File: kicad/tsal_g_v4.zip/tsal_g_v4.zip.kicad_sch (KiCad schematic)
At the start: 91 parts, among them J1 Conn_01x02_Pin, J2 Conn_01x02_Pin, J3 Conn_01x06_Pin, J6 Conn_01x02_Pin, J7 Conn_01x02_Pin, J8 Conn_01x03, Q1 2N7002, Q2 NCE60P04R, U1 TL431DBZ, U10 BU4S01G2, U11 BU4S01G2, U14 BUS4S71G2, U15 BUS4S71G2, U16 BU4SU69G2, U17 40106, U18 BU4S01G2, U19 BU4S01G2, U2 LTV-817S, U20 4071, U3 B1212, U4 BU4SU69G2, U5 40106, U6 40106, U7 BU4S81G2

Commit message: updated tsal
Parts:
- removed C20: 0.1uF, Capacitor_SMD:C_0805_2012Metric_Pad1.18x1.45mm_HandSolder, symbol Device:C
- removed D8: LED, LED_SMD:LED_0805_2012Metric_Pad1.15x1.40mm_HandSolder, symbol Device:LED
- removed Q2: NCE60P04R, Package_TO_SOT_SMD:SOT-223-3_TabPin2, symbol Transistor_FET:AO3401A
- removed R27: 1k, Resistor_SMD:R_0805_2012Metric_Pad1.20x1.40mm_HandSolder, symbol Device:R
- removed U15: BUS4S71G2, Package_TO_SOT_SMD:SOT-23-5_HandSoldering, symbol 74xGxx:74AHC1G32
- removed U17: 40106, to be sorted:SOIC-14_3.9x8.7mm_P1.27mm_extendedpad, symbol 4xxx:40106
- removed U18, U19: BU4S01G2, Package_TO_SOT_SMD:SOT-23-5_HandSoldering, symbol 74xGxx:74AHC1G02
- added D10: LED, RMC_LED:LED_0805_2012Metric_Pad1.45x1.40mm_HandSolder, symbol Device:LED
- added Q4: QM6015D, RMC_TO:TO-252-2, symbol Transistor_FET:QM6015D
- added R31: 1k, RMC_Resistor:R_0805_2012Metric_Pad1.20x1.40mm_HandSolder_L, symbol Device:R
- added U12: 4077, RMC_SO:SOIC127P600X175-14N, symbol 4xxx:4077
- added U13: BU4S71G2, symbol 74xGxx:74AHC1G32
- added U9: 40106, RMC_SO:SOIC127P600X175-14N, symbol 4xxx:40106
- C1, C11, C12, C15, C16, C17, C18, C19, C2, C21, C22, C23, C24, C3, C4, C5, C6, C7, C8, C9: footprint Capacitor_SMD:C_0805_2012Metric_Pad1.18x1.45mm_HandSolder -> RMC_Capacitor:C_0805_2012Metric_Pad1.18x1.45mm_HandSolder_L
- D2, D4, D5, D6, D7, D9: footprint LED_SMD:LED_0805_2012Metric_Pad1.15x1.40mm_HandSolder -> RMC_LED:LED_0805_2012Metric_Pad1.45x1.40mm_HandSolder
- D3: footprint Diode_SMD:D_SMA -> Diode_SMD:D_SMA_Handsoldering
- F2: footprint Fuse:Fuse_1210_3225Metric_Pad1.42x2.65mm_HandSolder -> to be sorted:Fuse_1210_3225Metric_Pad1.42x2.65mm_HandSolder
- LM1: footprint Package_SO:SOIC-8_3.9x4.9mm_P1.27mm -> RMC_SO:SOIC-8_3.9x4.9mm_P1.27mm_RMC_Handsolder
- Q1, U1: footprint Package_TO_SOT_SMD:SOT-23_Handsoldering -> RMC_SOT:SOT-23
- R1, R10, R11, R12, R13, R14, R15, R16, R17, R18, R19, R2, R20, R21, R22, R23, R24, R25, R26, R28, R29, R3, R30, R4, R5, R6, R7, R8, R9: footprint Resistor_SMD:R_0805_2012Metric_Pad1.20x1.40mm_HandSolder -> RMC_Resistor:R_0805_2012Metric_Pad1.20x1.40mm_HandSolder_L
- U10, U11, U14, U16, U7: footprint Package_TO_SOT_SMD:SOT-23-5_HandSoldering -> RMC_SOT:SOT-23-5_HandSoldering_Extended_RMC
- U20, U5, U6: footprint to be sorted:SOIC-14_3.9x8.7mm_P1.27mm_extendedpad -> RMC_SO:SOIC127P600X175-14N
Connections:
- net AIRH Check: now also U20.3, U20.9; no longer U20.2, U20.4
- net AIRL Check: now also U20.11; no longer U20.10
- net GLV+: now also Q4.3 (S)
- net GLV-: now also C19.2, U16.5 (VCC), R31.2, U12.6, U12.7 (VSS), U13.3 (GND), U9.7 (VSS); no longer C19.1, U16.3 (GND)
- net GRN+: now also D10.2 (A), Q4.2 (D)
- net Out +: now also U20.12; no longer U20.8
- net Out -: now also U20.1; no longer U20.5
- net Out Precharge: now also U20.6; no longer U20.13
- net Precharge Check: now also U20.4, U20.8; no longer U20.1, U20.11
- net RELAY RESET: now also U13.2
- net RESET: now also U12.1, U12.4
- net TS RESET: now also U13.1
- net VCC: now also C19.1, U16.3 (GND), U12.14 (VDD), U13.5 (VCC), U9.14 (VDD); no longer C19.2, U16.5 (VCC)
- net high aux: now also U20.2; no longer U20.6
- net low aux: now also U20.13; no longer U20.9
- net pre aux: now also U20.5; no longer U20.12
- net at U10.4, U11.1: now also Q4.1 (G)
- net at C16.2, R29.1: now also U9.1
- net at U14.2: now also U20.10; no longer U20.3
- new net: U12.3, U12.5, U9.12
- new net: U9.13, U9.2
- new net: D10.1 (K), R31.1
- new net: U12.2, U13.4
- no-connect marks 0 -> 14
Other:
- moved on the sheet: C16, C17, R28, R29, U20A, U20B, U20C, U20D

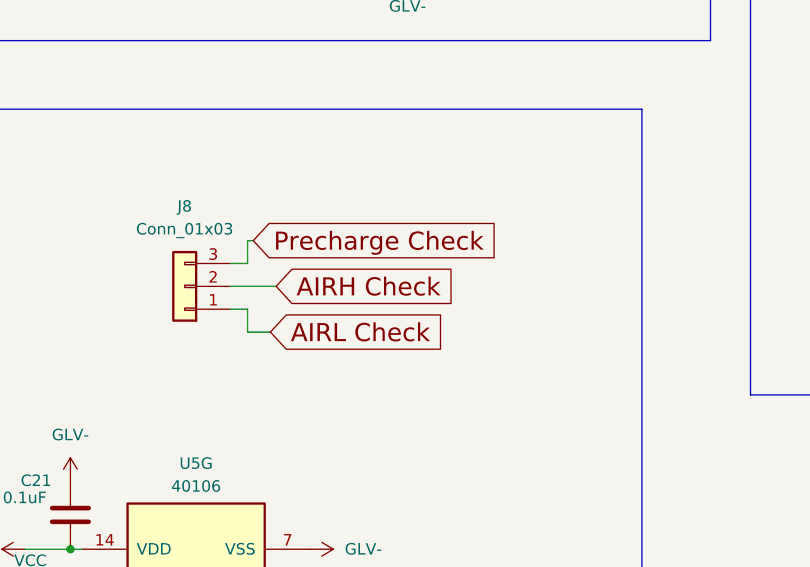
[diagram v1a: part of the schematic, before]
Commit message: Plausibility check and ERC debug
-inverted plausibility check pin out
-arrange silkscreen reference
-debug ERC
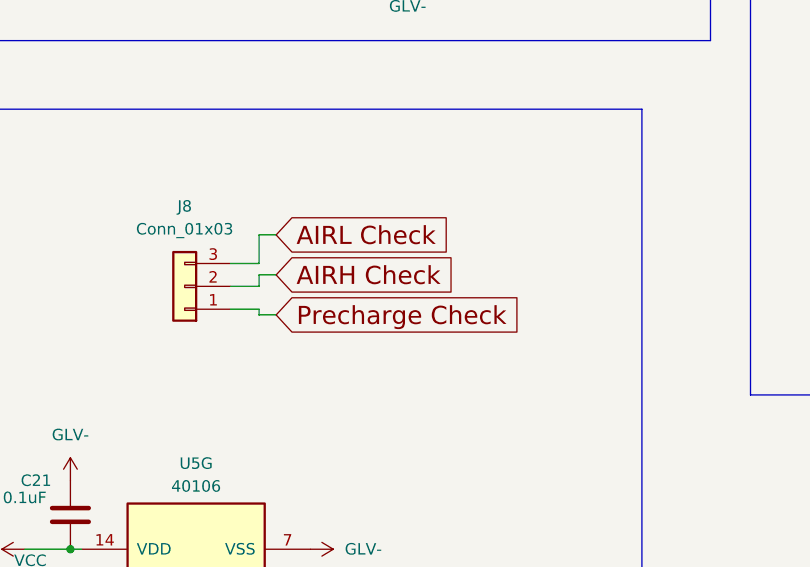
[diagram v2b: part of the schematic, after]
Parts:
- U13: footprint (none) -> RMC_SOT:SOT-23-5_HandSoldering_Extended_RMC
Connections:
- net AIRL Check: now also J8.3 (Pin_3); no longer J8.1 (Pin_1)
- net Precharge Check: now also J8.1 (Pin_1); no longer J8.3 (Pin_3)
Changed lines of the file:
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@@
 	(wire
 		(pts
+			(xy 354.33 305.435) (xy 354.33 306.705)
+		)
+		(stroke
+			(width 0)
+			(type default)
+		)
+	)
+	(wire
+		(pts
 			(xy 86.36 116.84) (xy 104.14 116.84)
 		)
@@
 	(wire
 		(pts
-			(xy 353.06 311.785) (xy 355.6 311.785)
-		)
-		(stroke
-			(width 0)
-			(type default)
-		)
-	)
-	(wire
-		(pts
 			(xy 121.92 171.45) (xy 124.46 171.45)
 		)
@@
 	(wire
 		(pts
-			(xy 353.06 304.165) (xy 351.155 304.165)
-		)
-		(stroke
-			(width 0)
-			(type default)
-		)
-	)
-	(wire
-		(pts
 			(xy 226.695 353.695) (xy 238.76 353.695)
 		)
@@
 	(wire
 		(pts
-			(xy 356.235 306.705) (xy 351.155 306.705)
+			(xy 356.235 305.435) (xy 354.33 305.435)
 		)
 		(stroke
@@
 	(wire
 		(pts
-			(xy 351.155 309.245) (xy 353.06 309.245)
+			(xy 354.33 309.88) (xy 356.235 309.88)
 		)
 		(stroke
@@
 	(wire
 		(pts
+			(xy 354.33 304.165) (xy 351.155 304.165)
+		)
+		(stroke
+			(width 0)
+			(type default)
+		)
+	)
+	(wire
+		(pts
 			(xy 345.44 234.95) (xy 345.44 254)
 		)
@@
 	(wire
 		(pts
-			(xy 353.695 301.625) (xy 353.06 301.625)
-		)
-		(stroke
-			(width 0)
-			(type default)
-		)
-	)
-	(wire
-		(pts
 			(xy 226.695 339.09) (xy 226.695 353.695)
 		)
@@
 	(wire
 		(pts
+			(xy 354.33 309.245) (xy 351.155 309.245)
+		)
+		(stroke
+			(width 0)
+			(type default)
+		)
+	)
+	(wire
+		(pts
 			(xy 378.46 114.3) (xy 376.555 114.3)
 		)
@@
 	(wire
 		(pts
+			(xy 354.33 309.88) (xy 354.33 309.245)
+		)
+		(stroke
+			(width 0)
+			(type default)
+		)
+	)
+	(wire
+		(pts
 			(xy 53.34 194.31) (xy 67.31 194.31)
 		)
@@
 	(wire
 		(pts
+			(xy 354.33 306.705) (xy 351.155 306.705)
+		)
+		(stroke
+			(width 0)
+			(type default)
+		)
+	)
+	(wire
+		(pts
 			(xy 488.95 256.54) (xy 487.68 256.54)
 		)
@@
 	(wire
 		(pts
-			(xy 353.06 301.625) (xy 353.06 304.165)
+			(xy 67.31 194.31) (xy 67.31 198.12)
 		)
 		(stroke
@@
 	(wire
 		(pts
-			(xy 67.31 194.31) (xy 67.31 198.12)
+			(xy 354.33 300.99) (xy 354.33 304.165)
 		)
 		(stroke
@@
 	(wire
 		(pts
-			(xy 227.33 111.76) (xy 227.33 131.445)
+			(xy 356.235 300.99) (xy 354.33 300.99)
 		)
 		(stroke
@@
 	(wire
 		(pts
-			(xy 210.82 194.945) (xy 210.82 195.58)
+			(xy 227.33 111.76) (xy 227.33 131.445)
 		)
 		(stroke
@@
 	(wire
 		(pts
-			(xy 528.32 259.08) (xy 542.925 259.08)
+			(xy 210.82 194.945) (xy 210.82 195.58)
 		)
 		(stroke
@@
 		)
 	)
-	(polyline
+	(wire
 		(pts
-			(xy 49.53 149.86) (xy 49.53 204.47)
+			(xy 528.32 259.08) (xy 542.925 259.08)
 		)
 		(stroke
 			(width 0)
-			(type dash)
+			(type default)
 		)
 	)
-	(wire
+	(polyline
 		(pts
-			(xy 353.06 309.245) (xy 353.06 311.785)
+			(xy 49.53 149.86) (xy 49.53 204.47)
 		)
 		(stroke
 			(width 0)
-			(type default)
+			(type dash)
 		)
 	)
@@
 		)
 	)
-	(global_label "AIRH Check"
+	(global_label "AIRL Check"
 		(shape input)
-		(at 356.235 306.705 0)
+		(at 425.45 67.945 0)
 		(fields_autoplaced yes)
 		(effects
@@
 		)
 		(property "Intersheetrefs" "${INTERSHEET_REFS}"
-			(at 378.1501 306.705 0)
+			(at 446.8873 67.945 0)
 			(effects
 				(font
@@
 	(global_label "AIRL Check"
 		(shape input)
-		(at 425.45 67.945 0)
+		(at 356.235 300.99 0)
 		(fields_autoplaced yes)
 		(effects
@@
 		)
 		(property "Intersheetrefs" "${INTERSHEET_REFS}"
-			(at 446.8873 67.945 0)
+			(at 377.6723 300.99 0)
 			(effects
 				(font
@@
 		)
 	)
-	(global_label "AIRL Check"
+	(global_label "Precharge Check"
 		(shape input)
-		(at 355.6 311.785 0)
+		(at 356.235 309.88 0)
 		(fields_autoplaced yes)
 		(effects
@@
 		)
 		(property "Intersheetrefs" "${INTERSHEET_REFS}"
-			(at 377.0373 311.785 0)
+			(at 386.4631 309.88 0)
 			(effects
 				(font
@@
 	(global_label "AIRH Check"
 		(shape input)
+		(at 356.235 305.435 0)
+		(fields_autoplaced yes)
+		(effects
+			(font
+				(size 2.0066 2.0066)
+			)
+			(justify left)
+		)
+		(property "Intersheetrefs" "${INTERSHEET_REFS}"
+			(at 378.1501 305.435 0)
+			(effects
+				(font
+					(size 1.27 1.27)
+				)
+				(justify left)
+				(hide yes)
+			)
+		)
+	)
+	(global_label "AIRH Check"
+		(shape input)
 		(at 340.995 149.86 180)
 		(fields_autoplaced yes)
@@
 		)
 	)
-	(global_label "Precharge Check"
-		(shape input)
-		(at 353.695 301.625 0)
-		(fields_autoplaced yes)
-		(effects
-			(font
-				(size 2.0066 2.0066)
-			)
-			(justify left)
-		)
-		(property "Intersheetrefs" "${INTERSHEET_REFS}"
-			(at 383.9231 301.625 0)
-			(effects
-				(font
-					(size 1.27 1.27)
-				)
-				(justify left)
-				(hide yes)
-			)
-		)
-	)
 	(global_label "AIRL Check"
 		(shape input)
@@
 			)
 		)
-		(property "Footprint" ""
+		(property "Footprint" "RMC_SOT:SOT-23-5_HandSoldering_Extended_RMC"
 			(at 466.09 288.29 0)
 			(effects

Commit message: Updated plausibility latch logic
need review
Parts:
- removed C16, C17, C23: 0.1uF, RMC_Capacitor:C_0805_2012Metric_Pad1.18x1.45mm_HandSolder_L, symbol Device:C
- removed D2, D9: LED, RMC_LED:LED_0805_2012Metric_Pad1.45x1.40mm_HandSolder, symbol Device:LED
- removed R12, R30: 1k, RMC_Resistor:R_0805_2012Metric_Pad1.20x1.40mm_HandSolder_L, symbol Device:R
- removed R28: 10k, RMC_Resistor:R_0805_2012Metric_Pad1.20x1.40mm_HandSolder_L, symbol Device:R
- removed R29: 100k, RMC_Resistor:R_0805_2012Metric_Pad1.20x1.40mm_HandSolder_L, symbol Device:R
- removed U12: 4077, RMC_SO:SOIC127P600X175-14N, symbol 4xxx:4077
- removed U9: 40106, RMC_SO:SOIC127P600X175-14N, symbol 4xxx:40106
- added C13, C14, C20, C25: 0.1uF, RMC_Capacitor:C_0805_2012Metric_Pad1.18x1.45mm_HandSolder_L, symbol Device:C
- added U12, U15: BU4S01G2, RMC_SOT:SOT-23-5_HandSoldering_Extended_RMC, symbol 74xGxx:74AHC1G02
- added U17: BU4S71G2, RMC_SOT:SOT-23-5_HandSoldering_Extended_RMC, symbol 74xGxx:74AHC1G32
- added U21: 4071, RMC_SO:SOIC127P600X175-14N, symbol 4xxx:4071
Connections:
- net -HV is gone; now on net GND: J2.1 (Pin_1), J2.2 (Pin_2), R9.2
- net AIRH Check: now also U21.2
- net AIRL Check: now also U21.6
- net GLV-: now also C13.1, C14.1, C20.2, C25.1, U12.1, U12.3 (GND), U15.3 (GND), U17.3 (GND), U21.7 (VSS)
- net Precharge Check: now also U21.1
- net RESET: now also U17.4
- net VCC: now also C13.2, C14.2, C20.1, C25.2, U12.5 (VCC), U15.5 (VCC), U17.5 (VCC), U21.14 (VDD)
- net Vref: now also U1.2 (K); no longer U1.1 (K)
- net at R1.2, R2.1: now also U1.1 (REF); no longer U1.2 (REF)
- net at U13.4: now also U17.1
- new net: U21.3, U21.5
- new net: U12.2, U15.4
- new net: U12.4, U15.1, U17.2
- new net: U15.2, U21.4
- no-connect marks 14 -> 7
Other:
- note added: "Plausibility Reset Latch"
- note removed: "Power cycle Reset Latch"
- moved on the sheet: C19, U13

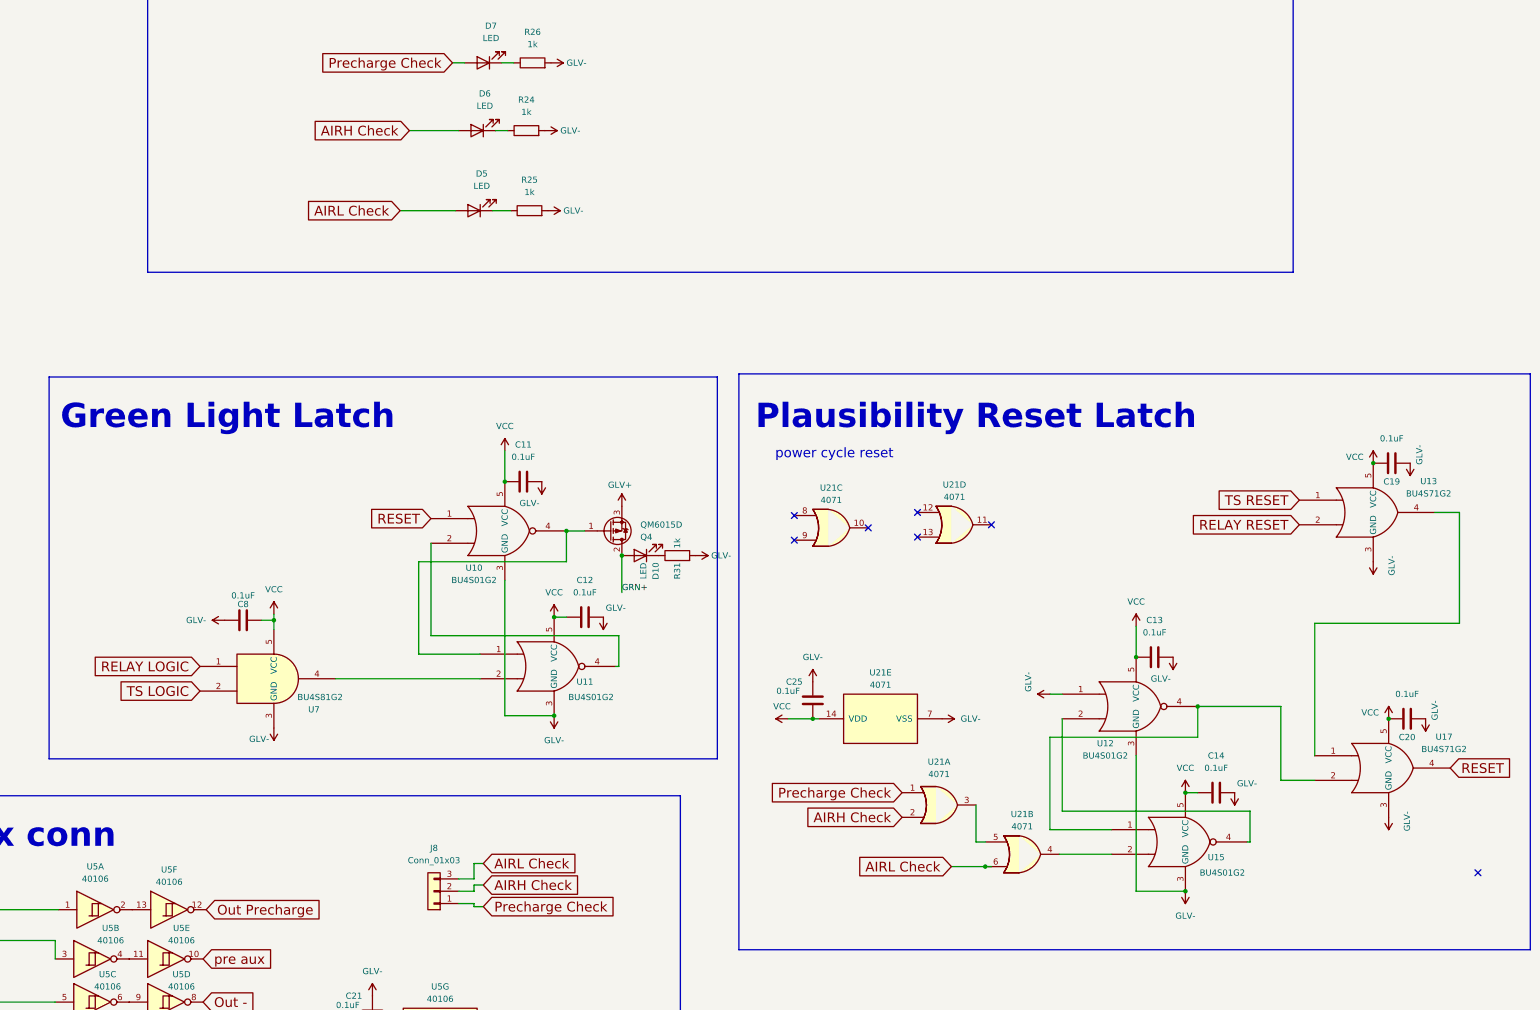
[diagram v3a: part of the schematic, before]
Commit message: updated cd4001
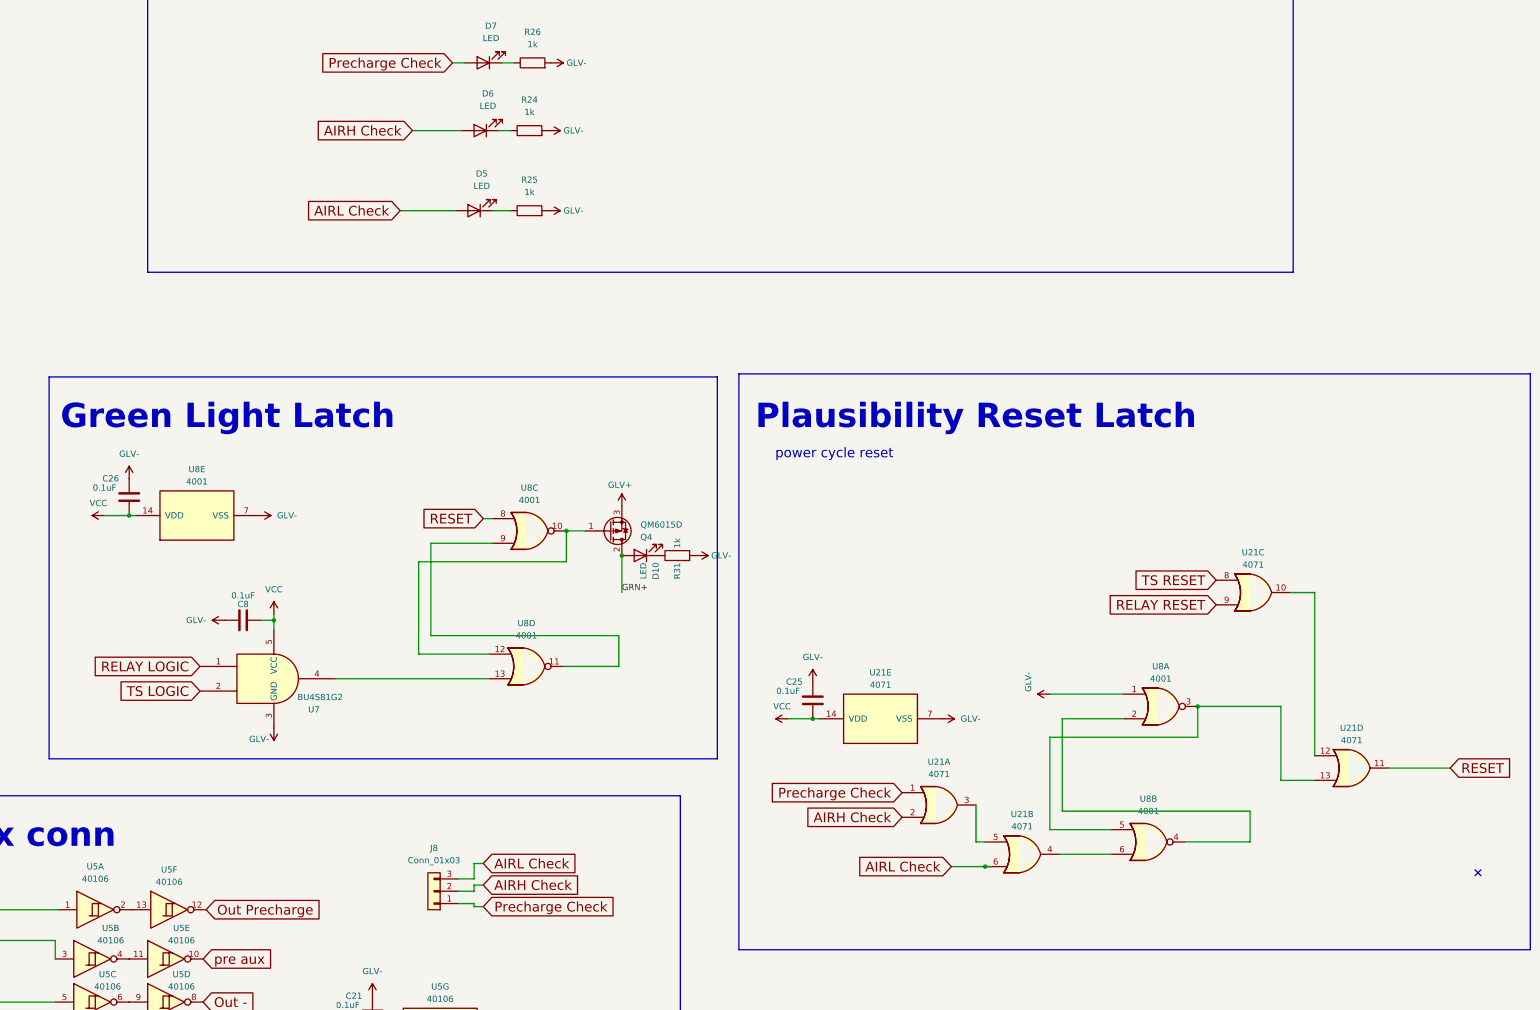
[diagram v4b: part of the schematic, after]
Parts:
- removed C11, C12, C13, C14, C19, C20: 0.1uF, RMC_Capacitor:C_0805_2012Metric_Pad1.18x1.45mm_HandSolder_L, symbol Device:C
- removed U10, U11, U12, U15: BU4S01G2, RMC_SOT:SOT-23-5_HandSoldering_Extended_RMC, symbol 74xGxx:74AHC1G02
- removed U13, U17: BU4S71G2, RMC_SOT:SOT-23-5_HandSoldering_Extended_RMC, symbol 74xGxx:74AHC1G32
- added C26: 0.1uF, RMC_Capacitor:C_0805_2012Metric_Pad1.18x1.45mm_HandSolder_L, symbol Device:C
- added U8: 4001, RMC_SO:SOIC127P600X175-14N, symbol 4xxx:4001
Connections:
- net GLV-: now also C26.1, U8.1, U8.7 (VSS)
- net RELAY RESET: now also U21.9
- net RESET: now also U21.11, U8.8
- net TS RESET: now also U21.8
- net VCC: now also C26.2, U8.14 (VDD)
- net at U21.12: now also U21.10
- net at U21.13: now also U8.3, U8.5
- net at Q4.1 (G): now also U8.10, U8.12
- net at U7.4: now also U8.13
- net at U21.4: now also U8.6
- new net: U8.11, U8.9
- new net: U8.2, U8.4
- no-connect marks 7 -> 1
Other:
- moved on the sheet: D6, R24, U21C, U21D
